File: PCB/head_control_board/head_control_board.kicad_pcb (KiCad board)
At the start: 2 copper layers, 104.5 x 72.5 mm, 59 parts, among them Q1 AO3401A, U1 TPS63070RNMR, U2 TPS63070RNMR, U3 SN74AHCT245PWR, U4 ESP32-S3-WROOM-1(N16R8)

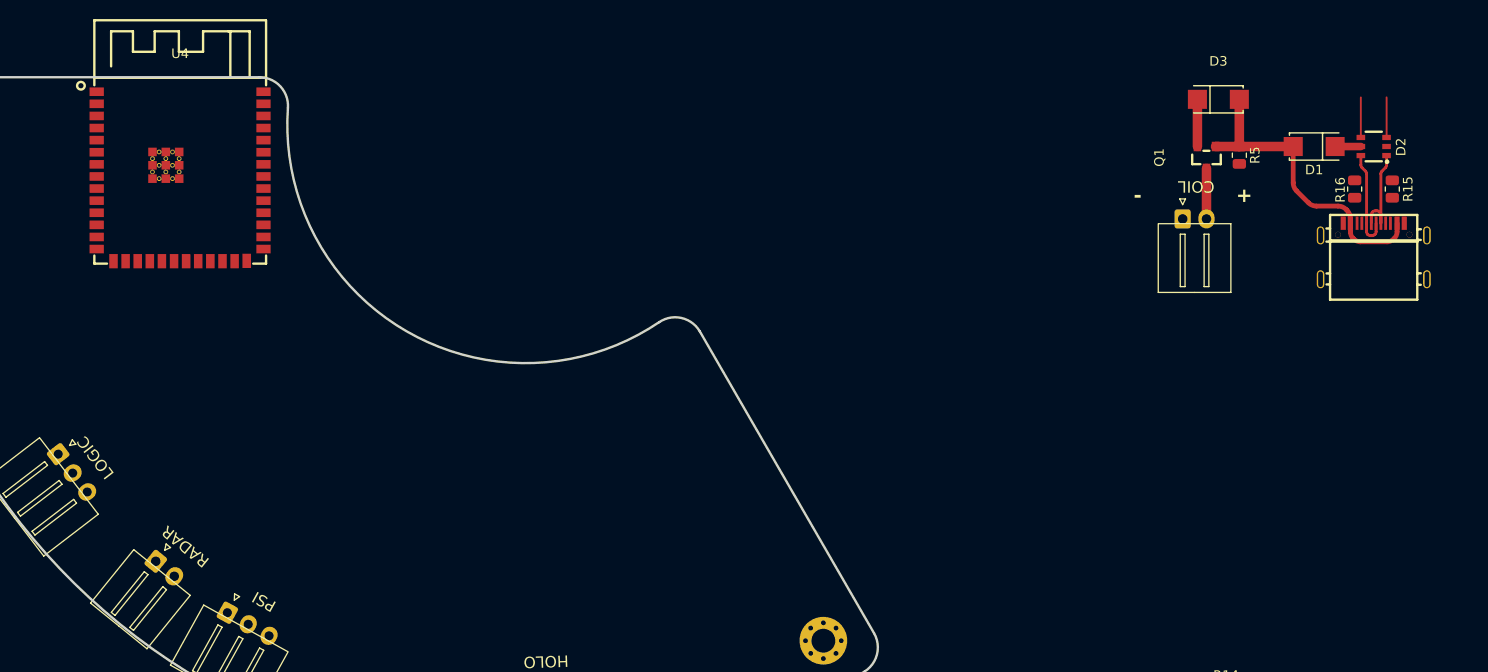
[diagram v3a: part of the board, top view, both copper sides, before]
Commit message: Finish USB differential routing
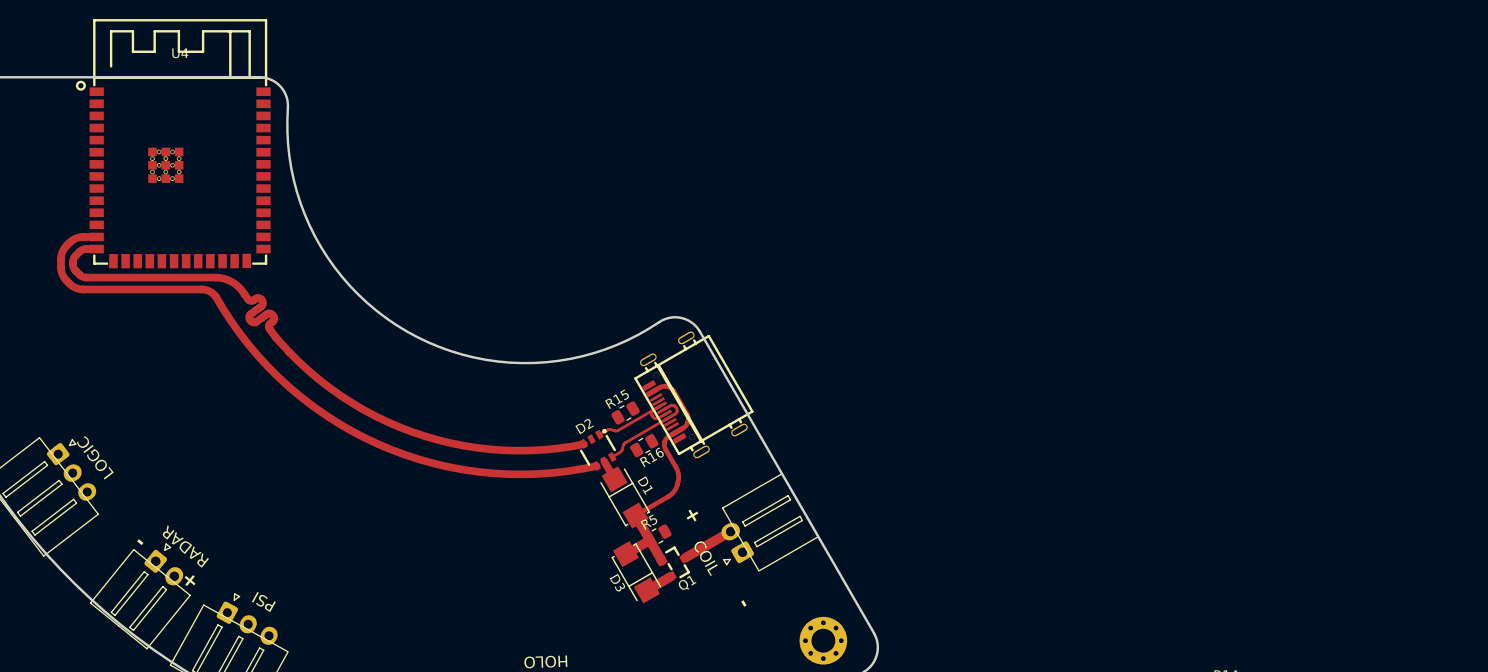
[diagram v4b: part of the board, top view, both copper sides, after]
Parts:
- moved D2 87.4 mm to (99.6, 64.6), turned to -150 degrees
- moved R15 83.8 mm to (102.5, 60.7), turned to 30 degrees
- moved D1 81.1 mm to (102.4, 69.6), turned to -60 degrees
- moved R16 79.3 mm to (104.5, 64.1), turned to 30 degrees
- moved D3 78.7 mm to (103.6, 77.4), turned to 120 degrees
- moved USBC1 73.5 mm to (109.1, 59.1), turned to 120 degrees
- moved R5 73.0 mm to (105.8, 73.6), turned to 30 degrees
- moved Q1 70.1 mm to (107.8, 76.5), turned to -150 degrees
- moved COIL1 57.9 mm to (114.8, 75.3), turned to 120 degrees
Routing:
- net /USB-D-: track 4.20 -> 67.9 mm
- net /USB-D+: track 4.20 -> 65.5 mm
- net Net-(Q1-G): track 33.2 -> 28.3 mm
- net +VIN: track 4.95 -> 2.90 mm
- net Net-(D1-Pad1): track 2.70 -> 2.15 mm

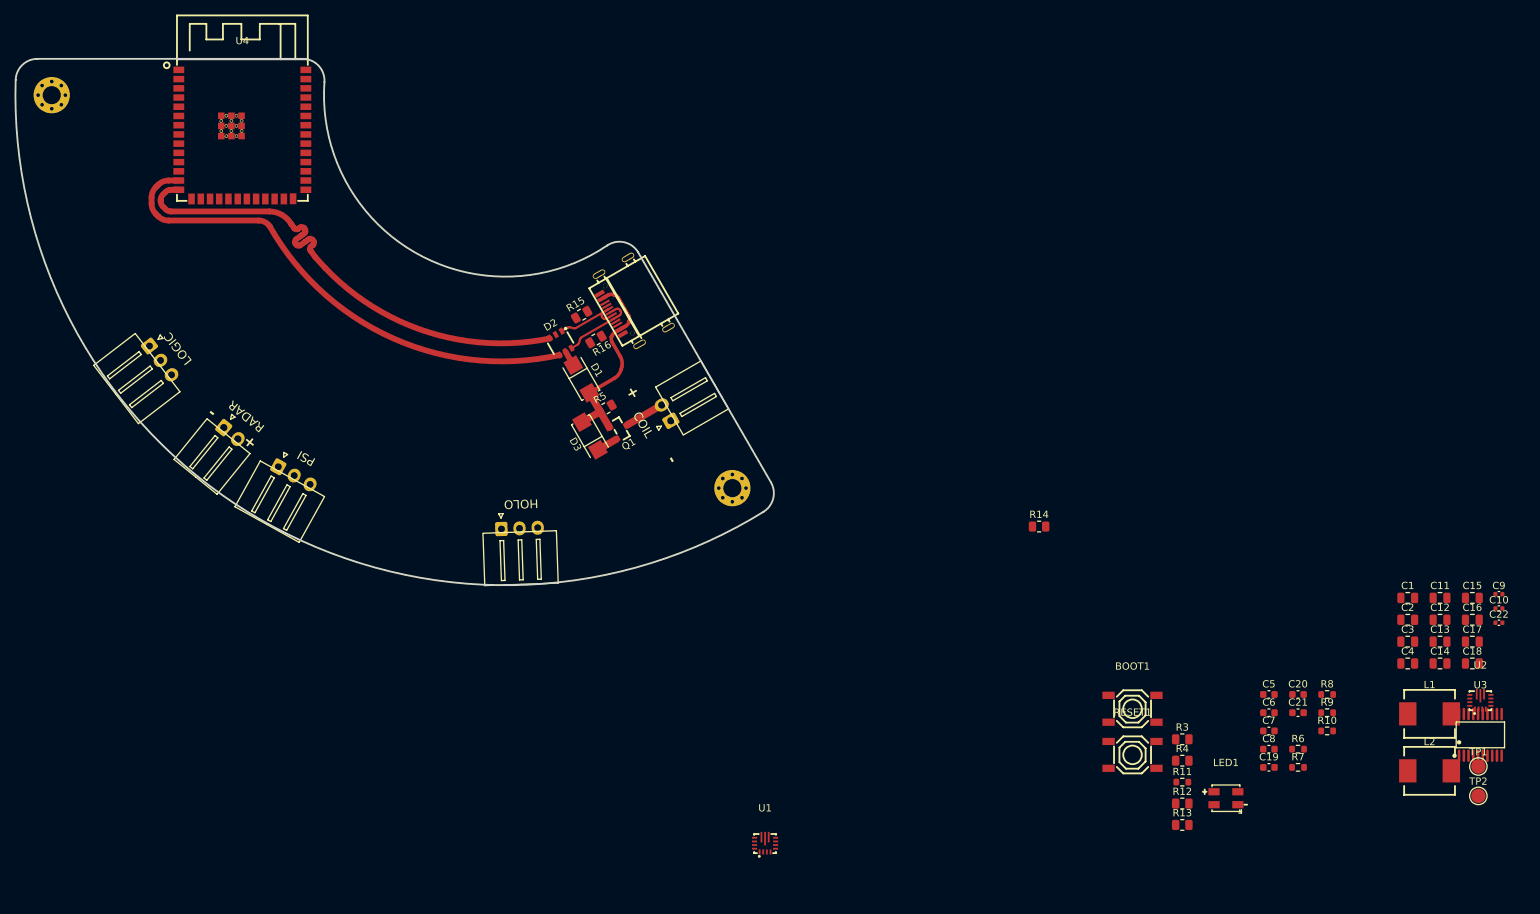
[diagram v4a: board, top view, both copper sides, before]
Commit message: Fillet tracks and update silkscreen
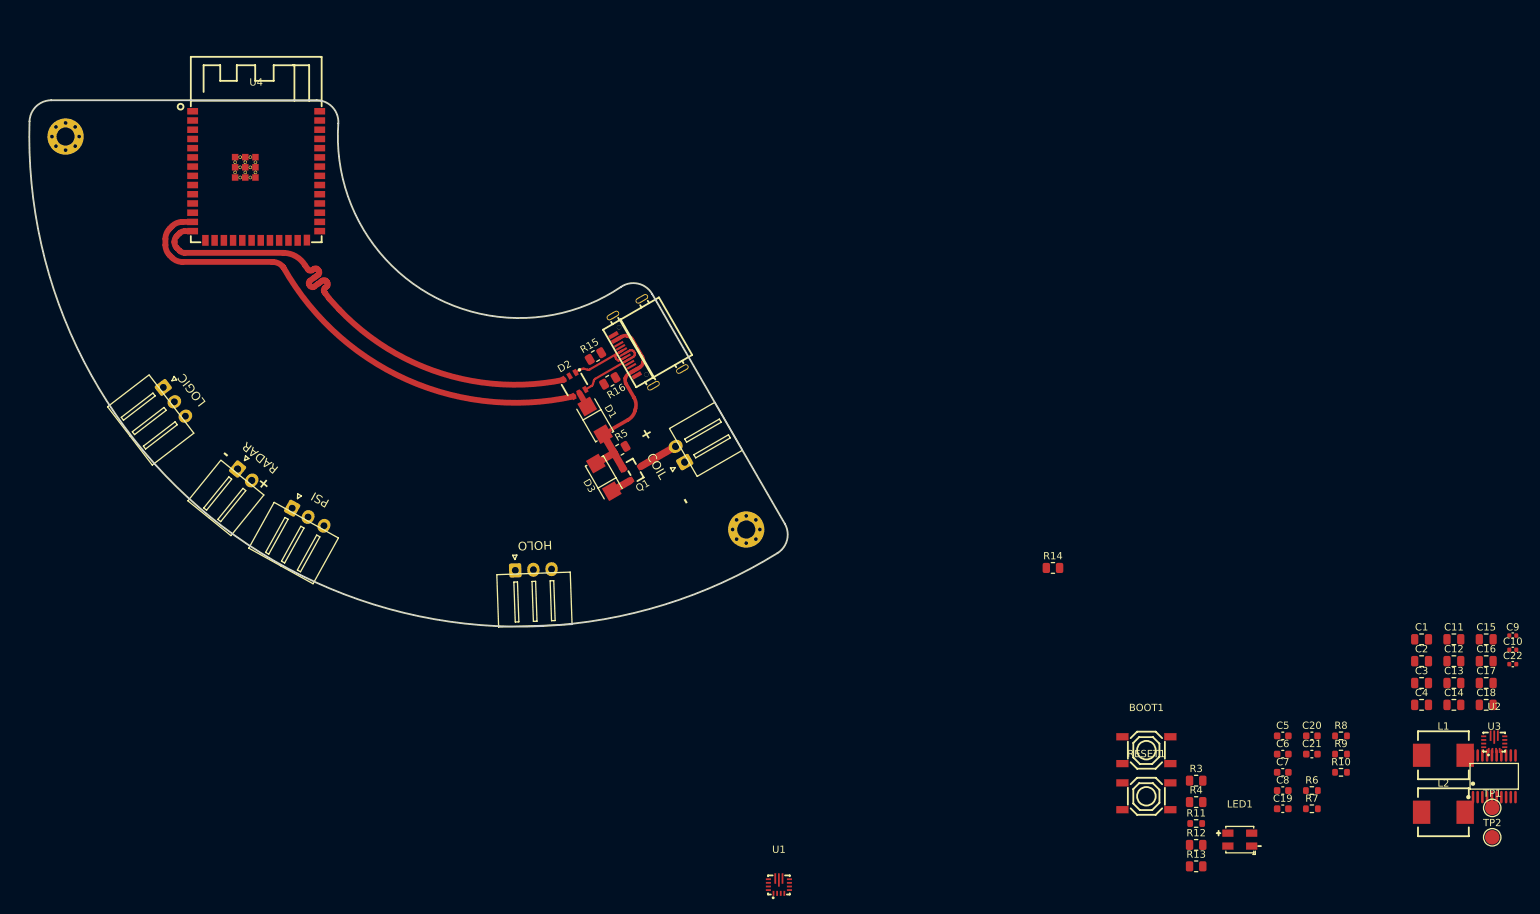
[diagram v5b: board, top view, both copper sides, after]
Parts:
- moved C19 6.01 mm to (199.1, 128.8)
- moved R11 6.01 mm to (187.1, 130.8)
- moved R7 6.01 mm to (203.1, 128.8)
- moved U1 6.01 mm to (129.7, 139.4)
- moved C15 6.01 mm to (227.1, 105.4)
- moved C16 6.01 mm to (227.1, 108.4)
- moved C17 6.01 mm to (227.1, 111.5)
- moved R10 6.01 mm to (207.1, 123.8)
- moved R8 6.01 mm to (207.1, 118.7)
- moved R5 6.01 mm to (107.7, 79.3)
- moved BOOT1 6.01 mm to (180.3, 120.7)
- moved C1 6.01 mm to (218.2, 105.4)
- moved C11 6.01 mm to (222.6, 105.4)
- moved C12 6.01 mm to (222.6, 108.4)
- moved C13 6.01 mm to (222.6, 111.5)
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
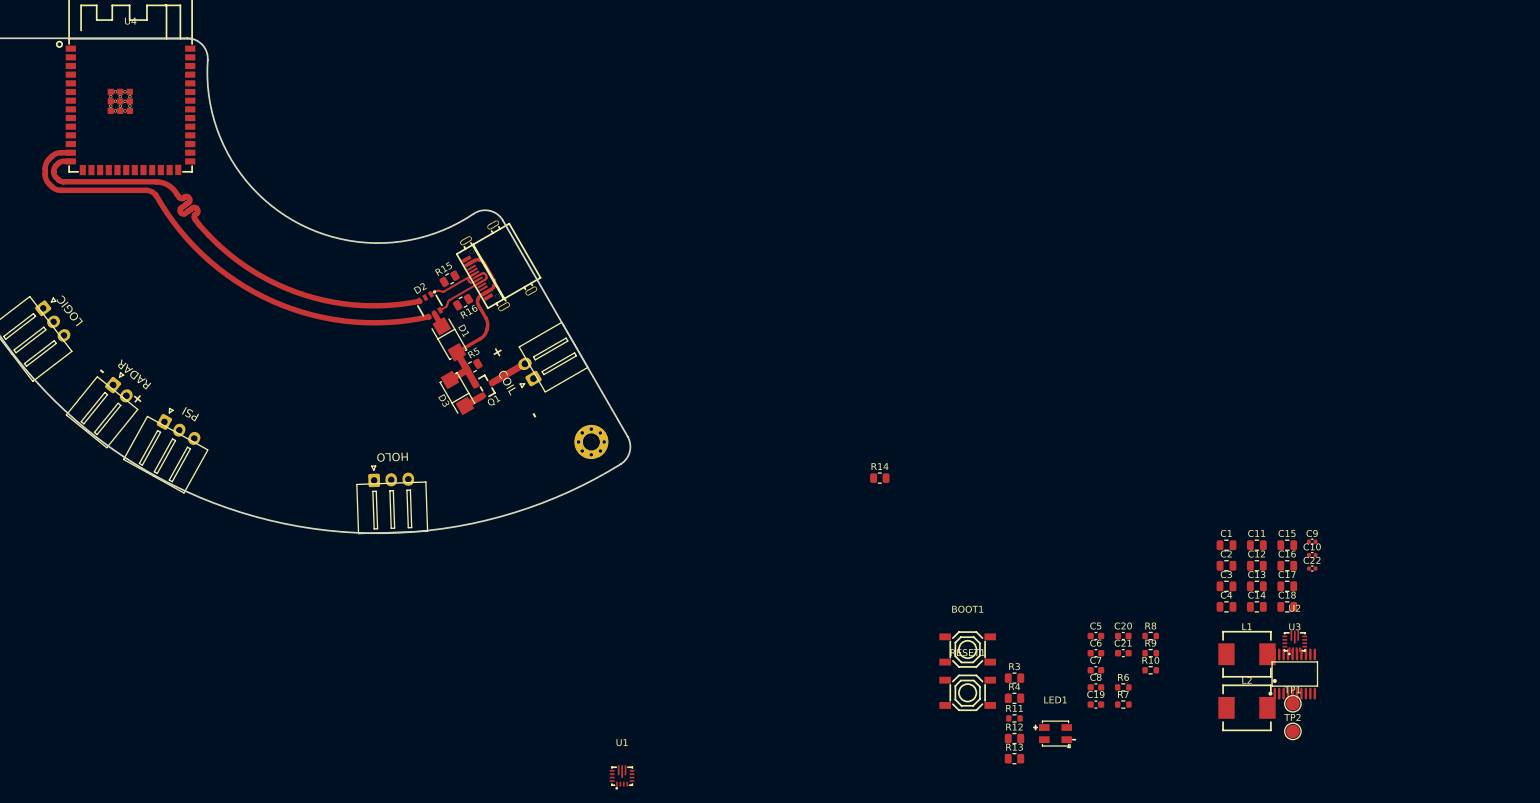
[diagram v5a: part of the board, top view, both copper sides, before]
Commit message: First pass on voltage regulators
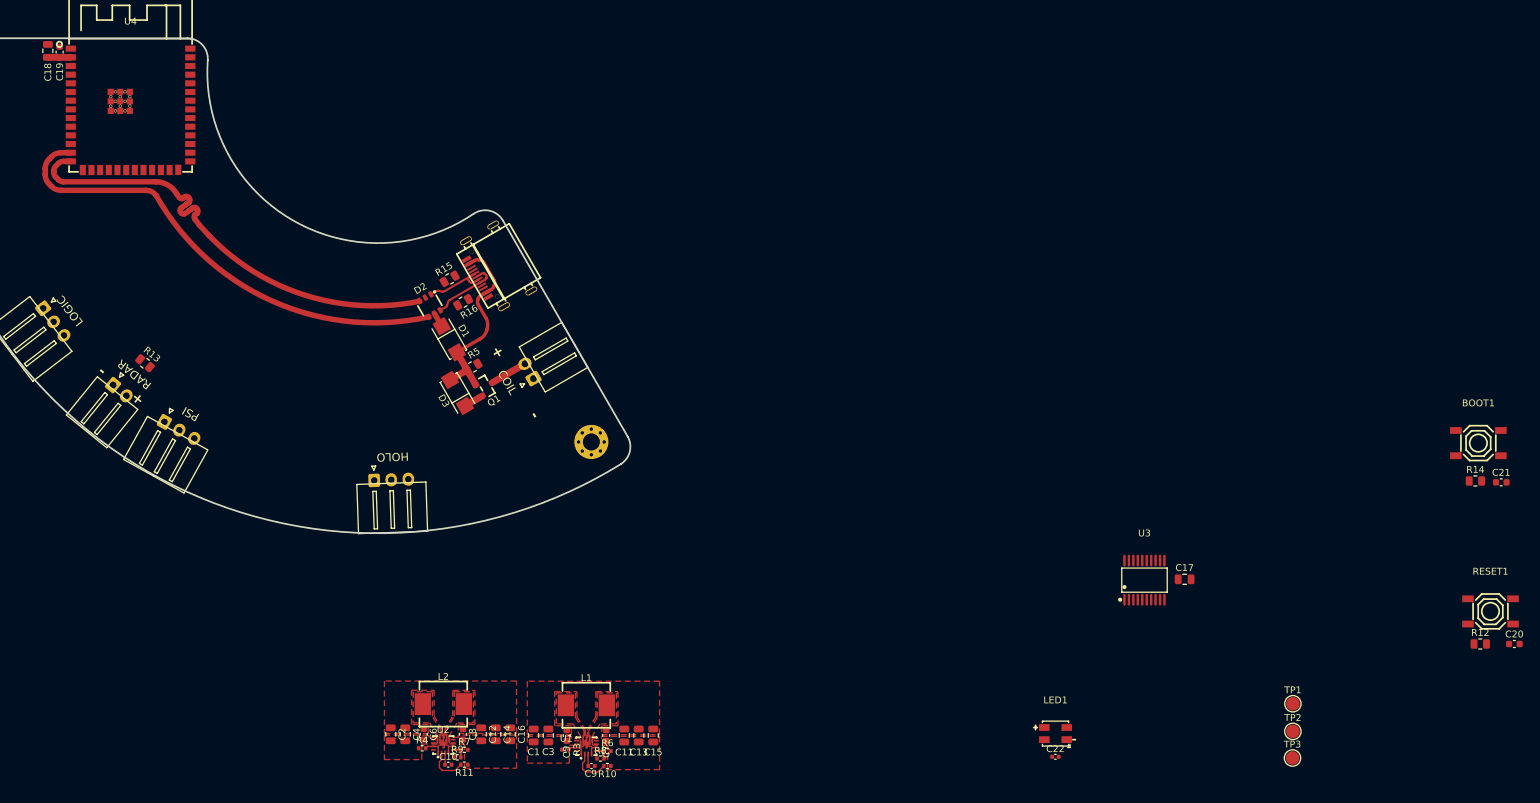
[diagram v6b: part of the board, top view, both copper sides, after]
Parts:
- added TP3: TestPoint, TestPoint:TestPoint_Pad_D2.0mm, F.Cu at (227.8, 136.6)
- R10, R11, R6, R7, R8, R9: footprint Resistor_SMD:R_0603_1608Metric -> Resistor_SMD:R_0402_1005Metric
- R3, R4: footprint Resistor_SMD:R_0805_2012Metric -> Resistor_SMD:R_0402_1005Metric
- moved C18 199.0 mm to (45.5, 33.0), turned to -90 degrees
- moved C19 179.4 mm to (47.3, 33.2), turned to -90 degrees
- moved R13 139.9 mm to (59.8, 78.8), turned to -39 degrees
- moved C10 130.2 mm to (104.2, 137.6)
- moved U2 125.6 mm to (103.5, 134.8)
- moved C2 124.9 mm to (95.8, 133.1), turned to -90 degrees
- moved C4 121.7 mm to (97.9, 133.1), turned to -90 degrees
- moved L2 117.7 mm to (103.5, 128.7)
- moved C16 116.4 mm to (113.3, 133.1), turned to -90 degrees
- moved C12 116.3 mm to (109.0, 133.1), turned to -90 degrees
- moved C14 113.0 mm to (111.2, 133.1), turned to -90 degrees
- moved C9 110.6 mm to (125.2, 137.8)
- moved C1 105.2 mm to (116.7, 133.3), turned to -90 degrees
- moved R9 102.7 mm to (105.5, 136.5)
- moved C3 101.7 mm to (118.8, 133.3), turned to -90 degrees
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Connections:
- U4 pad 10: unconnected-(U4-IO17-Pad10) -> /LED3_3V3
- U4 pad 11: unconnected-(U4-IO18-Pad11) -> /LED2_3V3
- U4 pad 12: unconnected-(U4-IO8-Pad12) -> /LED1_3V3
- U4 pad 19: /LED1_3V3 -> unconnected-(U4-IO11-Pad19)
- U4 pad 20: /LED2_3V3 -> unconnected-(U4-IO12-Pad20)
- U4 pad 21: /LED3_3V3 -> unconnected-(U4-IO13-Pad21)
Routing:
- net Net-(U2-PG): track 0.00 -> 5.95 mm
- net Net-(U1-PG): track 0.00 -> 5.95 mm
- net +3.3V: track 0.00 -> 3.36 mm
- net GND: track 0.00 -> 3.15 mm
- net Net-(U1-EN): track 0.00 -> 2.84 mm
- net Net-(U2-EN): track 0.00 -> 2.83 mm
- net Net-(U1-FB): track 0.00 -> 2.24 mm
- net Net-(U2-FB): track 0.00 -> 2.22 mm
- net Net-(U1-Vaux): track 0.00 -> 1.76 mm
- net Net-(U2-Vaux): track 0.00 -> 1.73 mm
- added copper zone on F.Cu, net +3.3V
- added copper zone on F.Cu, net +5V
- added copper zone on F.Cu, net +VIN
- added copper zone on F.Cu, net GND
- added copper zone on F.Cu, net Net-(U1-L1)
- added copper zone on F.Cu, net Net-(U1-L2)
- added copper zone on F.Cu, net Net-(U2-L1)
- added copper zone on F.Cu, net Net-(U2-L2)
